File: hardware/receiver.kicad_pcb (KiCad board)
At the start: 2 copper layers, 71.8 x 43.7 mm, 98 parts, among them J1 Conn_01x05_Male, J2 USB-C, J3 Left, J4 Right, Q1 S8050, Q2 S8050, Q3 AO3400A, Q4 AO3401A, SW1 Enable, SW2 Boot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

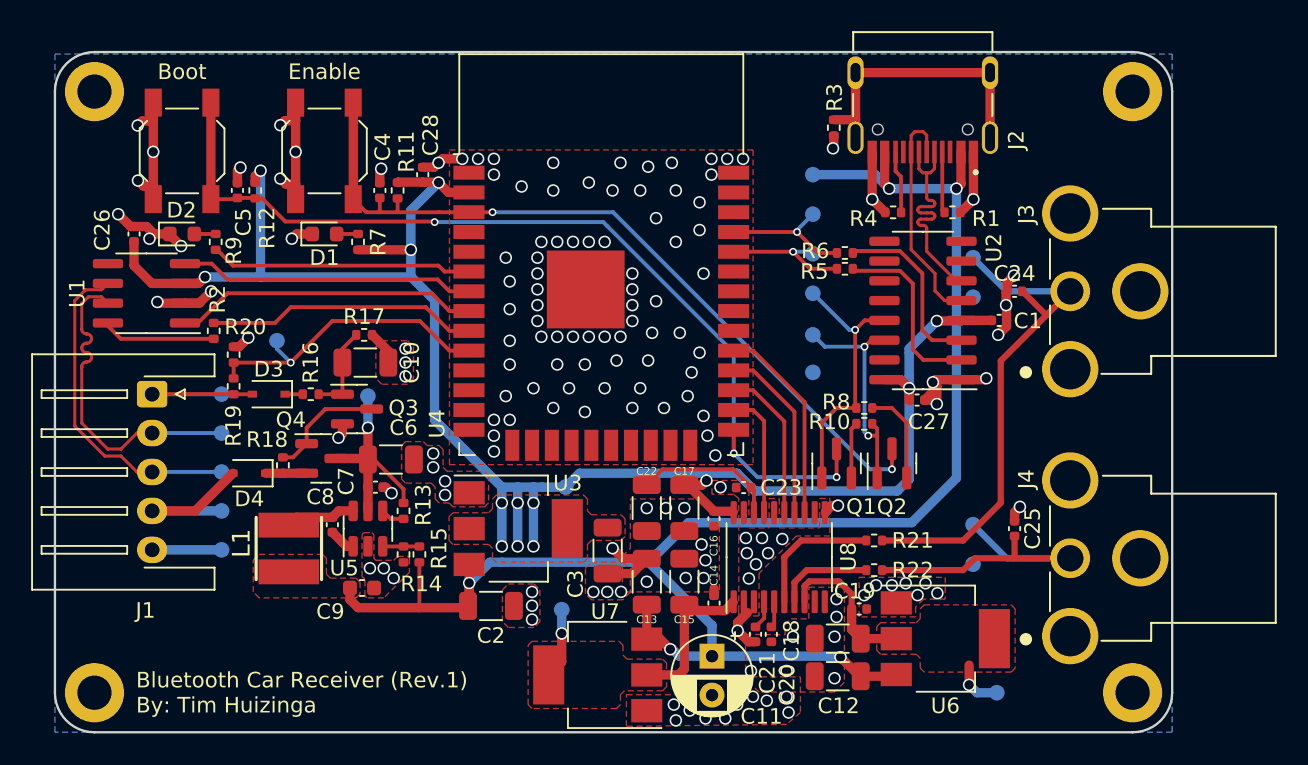
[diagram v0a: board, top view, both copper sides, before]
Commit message: Updated to new version of KiCad and made some small changes to the design
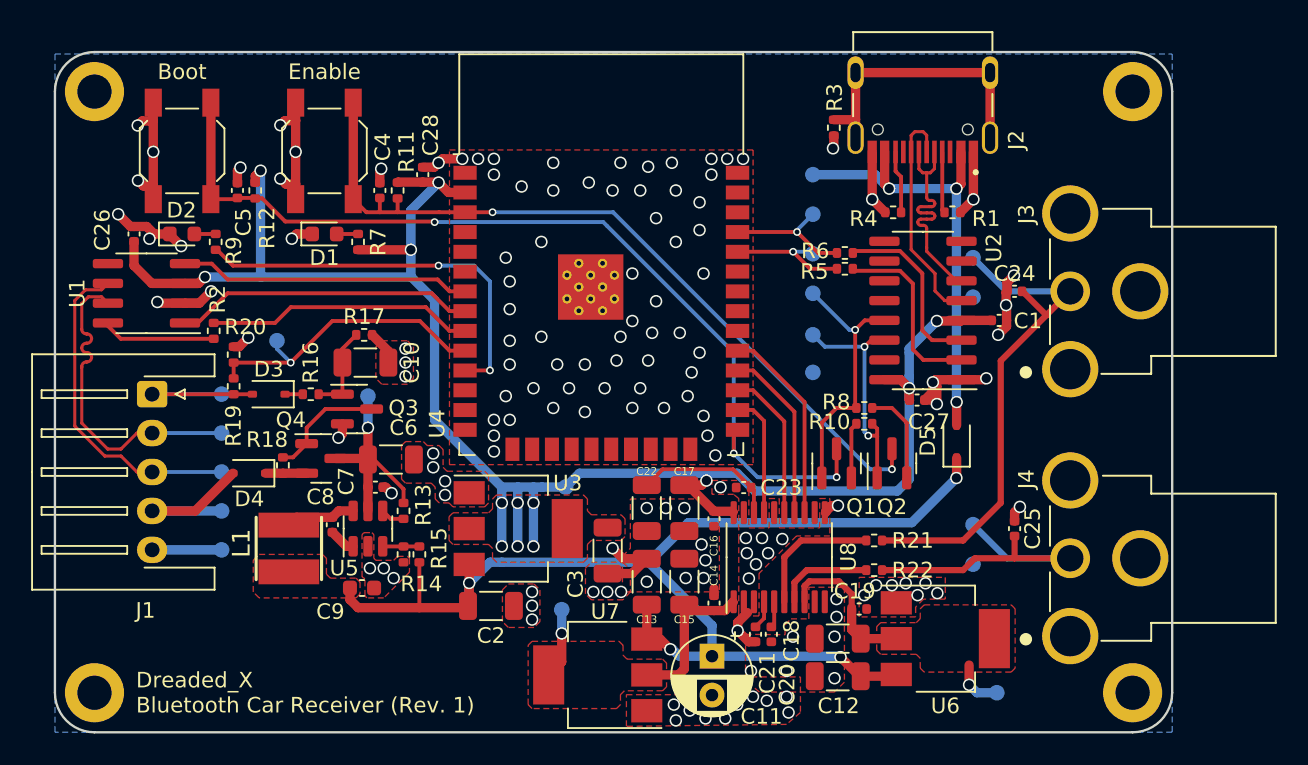
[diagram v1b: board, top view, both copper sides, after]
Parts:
- added D5: 1N5819WS, Diode_SMD:D_SOD-323, F.Cu at (108.4, 130.7)
- TP18: value 5V -> VBUS
- U4: value ESP32-WROOM-32E -> ESP32-WROOM-32
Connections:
- J2 pad A4B9: +5V -> /VBUS
- J2 pad B4A9: +5V -> /VBUS
- TP18 pad 1: +5V -> /VBUS
- U4 pad 11: unconnected-(U4-Pad11) -> /BLUE
- U4 pad 6: /BLUE -> unconnected-(U4-IO34-Pad6)
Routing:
- net +5V: track 110.1 -> 78.2 mm, vias 5 -> 4
- net /VBUS: track 0.00 -> 29.7 mm, vias 0 -> 3
- net /BLUE: track 16.8 -> 25.8 mm, vias 0 -> 2
- net GND: vias 163 -> 148
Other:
- board text added: "Dreaded_X Bluetooth Car Receiver (Rev. 1)"
- board text removed: "Bluetooth Car Receiver (Rev.1) By: Tim Huizinga"
